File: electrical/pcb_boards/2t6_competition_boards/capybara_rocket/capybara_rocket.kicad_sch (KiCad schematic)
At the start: 77 parts, among them J1 3.6V Battery, J10 Elevator, J11 SparkFun MAX-M10S, J12 Aileron 1, J13 Aileron 2, J14 Ground Camera, J15 Payload Camera, J16 DC Motor, J2 1.2V Battery, J3 3.6V Switch, J4 1.2V Switch, J5 LED, J6 NC, J7 CC, J8 VL53L1-SATEL, J9 Egg, U1 NE555P, U10 EEPROM, U11 STM32 NUCLEO-G431KB, U12 SparkFun XBee Explorer, U13 MAX756CPA+, U2 DS1307+, U3 Adafruit BNO085, U4 LTC3536, U5 MP3414, U6 Adafruit BMP581, U7 INA219, U8 DRV8212DRLR, U9 SN74LVC1G04DBVR, Y1 AB38T-32.768KHZ

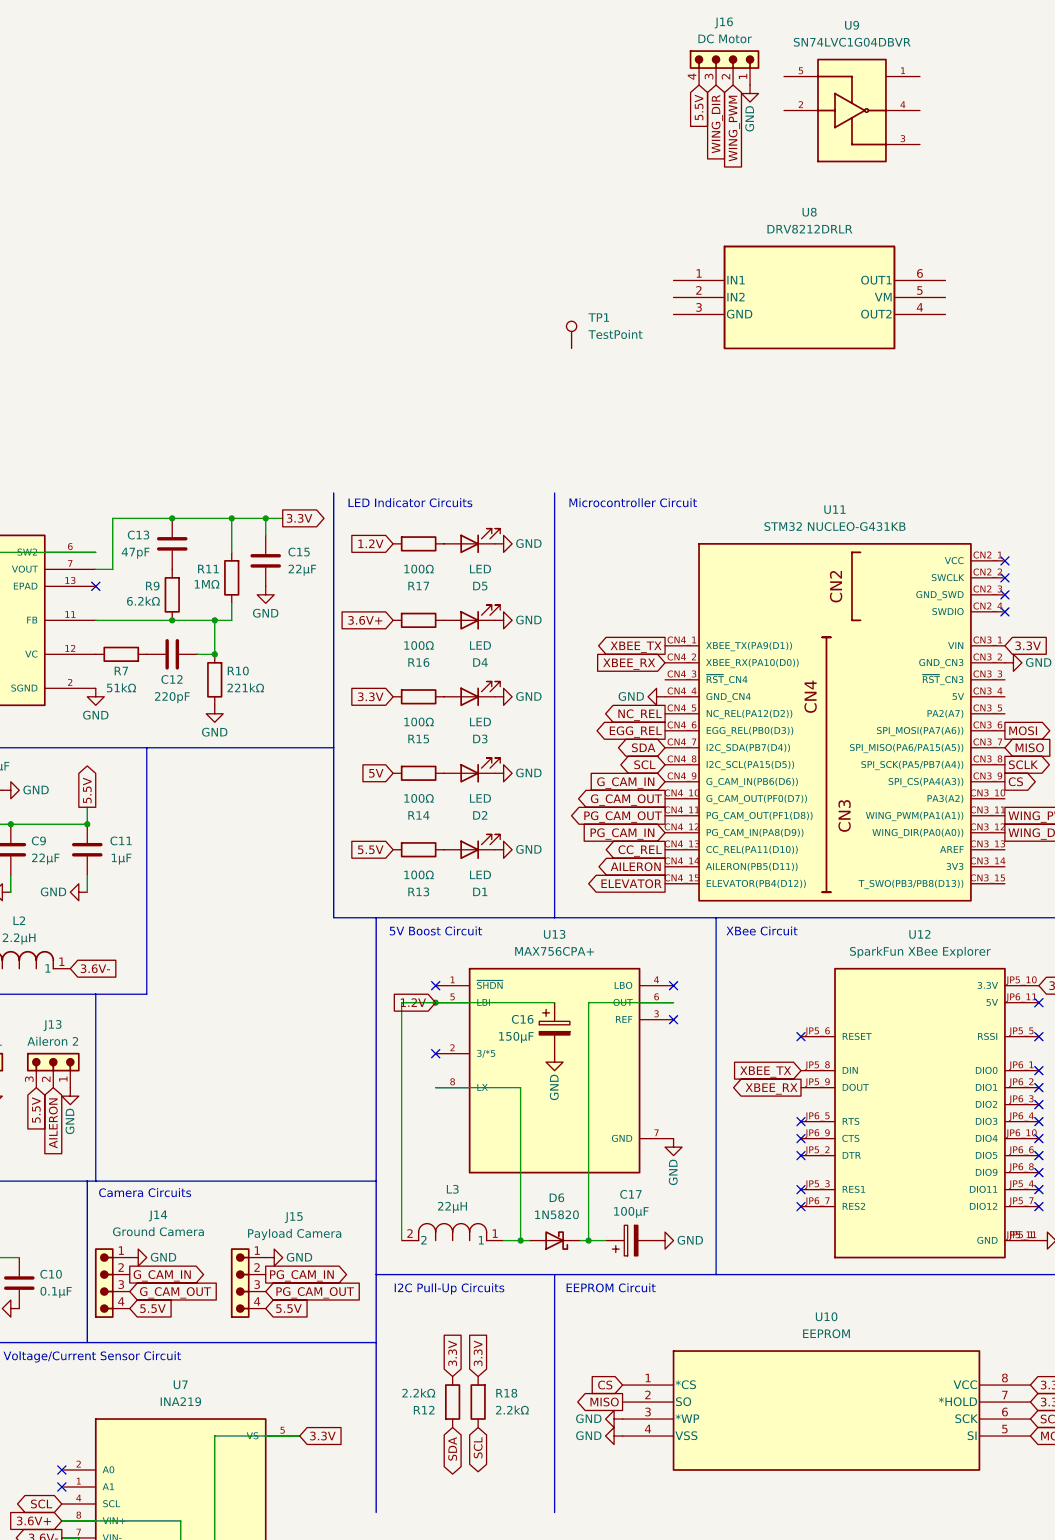
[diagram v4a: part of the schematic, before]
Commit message: Updates on component placements
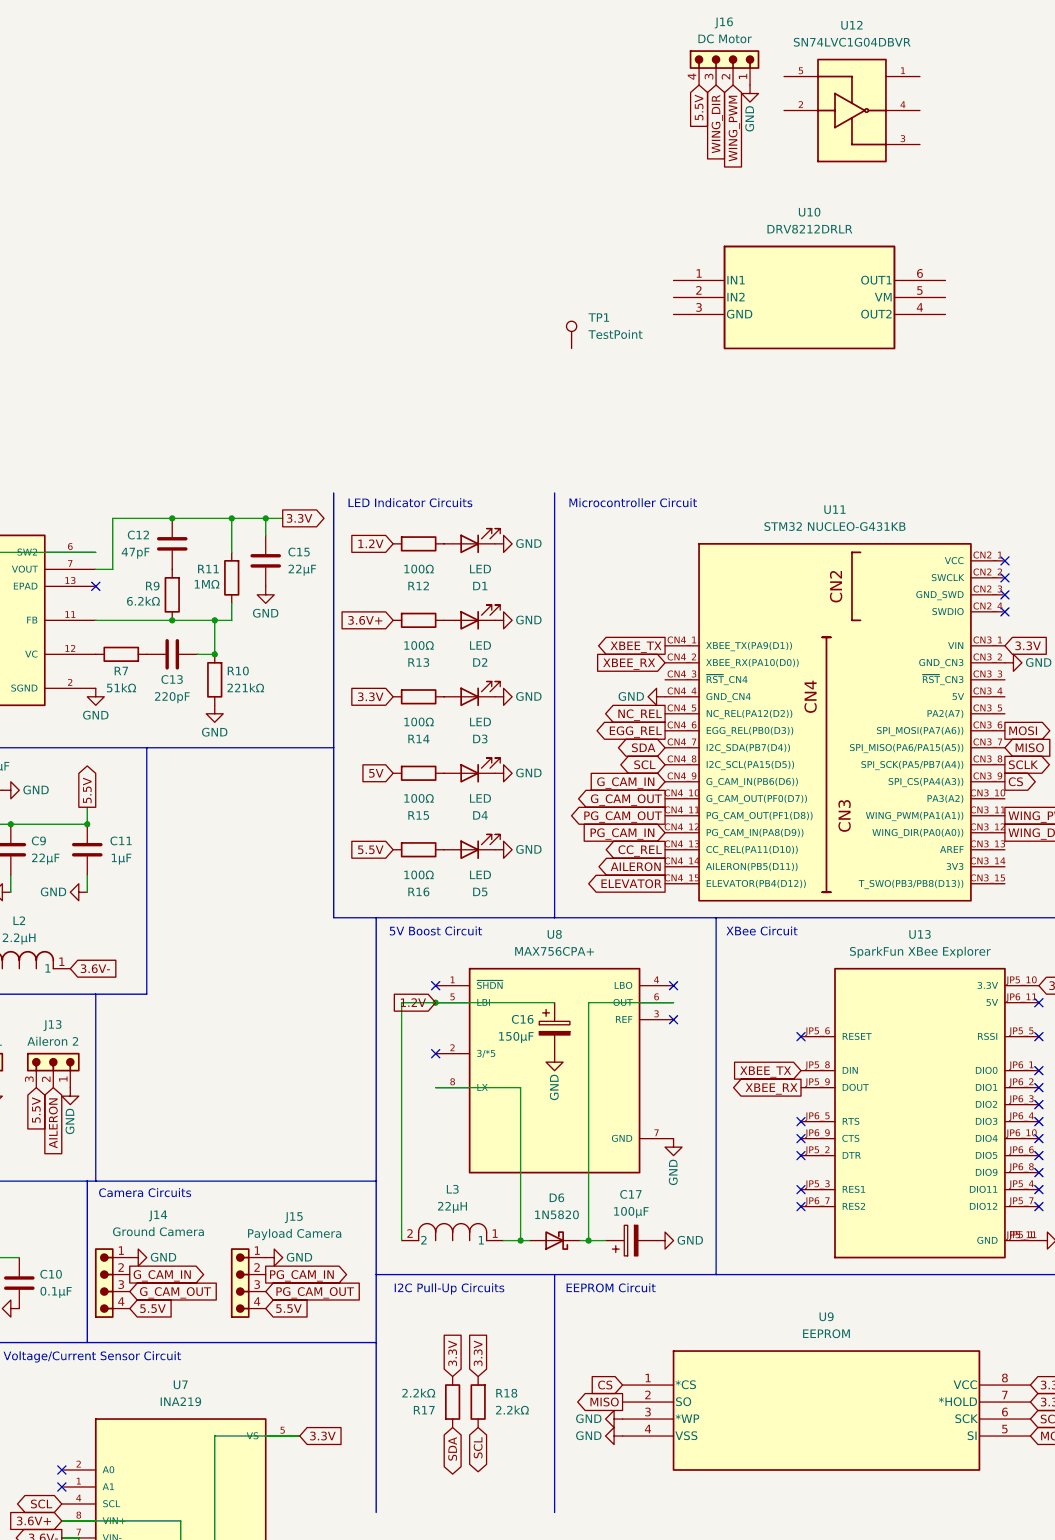
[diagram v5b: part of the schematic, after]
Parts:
- renumbered C13 to C12, C12 to C13, D5 to D1, D4 to D2, D2 to D4, D1 to D5, R17 to R12, R16 to R13, R15 to R14, R14 to R15, R13 to R16, R12 to R17, U8 to U10, U9 to U12, U12 to U13, U13 to U8, U10 to U9
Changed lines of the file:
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@@
 		(on_board yes)
 		(dnp no)
-		(property "Reference" "#PWR044"
+		(property "Reference" "#PWR048"
 			(at 200.66 66.04 0)
 			(effects
@@
 			(project "capybara_rocket"
 				(path "/401cca29-8a99-4116-a8ac-f330975a064c"
-					(reference "#PWR044")
+					(reference "#PWR048")
 					(unit 1)
 				)
@@
 		(on_board yes)
 		(dnp no)
-		(property "Reference" "#PWR040"
+		(property "Reference" "#PWR041"
 			(at 166.37 127 0)
 			(effects
@@
 			(project "capybara_rocket"
 				(path "/401cca29-8a99-4116-a8ac-f330975a064c"
-					(reference "#PWR040")
+					(reference "#PWR041")
 					(unit 1)
 				)
@@
 		(dnp no)
 		(fields_autoplaced yes)
-		(property "Reference" "D1"
+		(property "Reference" "D5"
 			(at 192.0875 72.39 0)
 			(effects
@@
 			(project ""
 				(path "/401cca29-8a99-4116-a8ac-f330975a064c"
-					(reference "D1")
+					(reference "D5")
 					(unit 1)
 				)
@@
 		(dnp no)
 		(fields_autoplaced yes)
-		(property "Reference" "U12"
+		(property "Reference" "U13"
 			(at 257.81 78.74 0)
 			(effects
@@
 			(project ""
 				(path "/401cca29-8a99-4116-a8ac-f330975a064c"
-					(reference "U12")
+					(reference "U13")
 					(unit 1)
 				)
@@
 		(on_board yes)
 		(dnp no)
-		(property "Reference" "R12"
+		(property "Reference" "R17"
 			(at 185.42 149.8601 0)
 			(effects
@@
 			(project "capybara_rocket"
 				(path "/401cca29-8a99-4116-a8ac-f330975a064c"
-					(reference "R12")
+					(reference "R17")
 					(unit 1)
 				)
@@
 		(dnp no)
 		(fields_autoplaced yes)
-		(property "Reference" "D2"
+		(property "Reference" "D4"
 			(at 192.0875 60.96 0)
 			(effects
@@
 			(project "capybara_rocket"
 				(path "/401cca29-8a99-4116-a8ac-f330975a064c"
-					(reference "D2")
+					(reference "D4")
 					(unit 1)
 				)
@@
 		(on_board yes)
 		(dnp no)
-		(property "Reference" "#PWR042"
+		(property "Reference" "#PWR040"
 			(at 160.02 33.02 0)
 			(effects
@@
 			(project "capybara_rocket"
 				(path "/401cca29-8a99-4116-a8ac-f330975a064c"
-					(reference "#PWR042")
+					(reference "#PWR040")
 					(unit 1)
 				)
@@
 		(on_board yes)
 		(dnp no)
-		(property "Reference" "#PWR049"
+		(property "Reference" "#PWR055"
 			(at 232.41 -41.91 0)
 			(effects
@@
 			(project "capybara_rocket"
 				(path "/401cca29-8a99-4116-a8ac-f330975a064c"
-					(reference "#PWR049")
+					(reference "#PWR055")
 					(unit 1)
 				)
@@
 		(on_board yes)
 		(dnp no)
-		(property "Reference" "#PWR055"
+		(property "Reference" "#PWR054"
 			(at 220.98 115.57 0)
 			(effects
@@
 			(project "capybara_rocket"
 				(path "/401cca29-8a99-4116-a8ac-f330975a064c"
-					(reference "#PWR055")
+					(reference "#PWR054")
 					(unit 1)
 				)
@@
 		(dnp no)
 		(fields_autoplaced yes)
-		(property "Reference" "D5"
+		(property "Reference" "D1"
 			(at 192.0875 26.67 0)
 			(effects
@@
 			(project "capybara_rocket"
 				(path "/401cca29-8a99-4116-a8ac-f330975a064c"
-					(reference "D5")
+					(reference "D1")
 					(unit 1)
 				)
@@
 		(dnp no)
 		(fields_autoplaced yes)
-		(property "Reference" "R13"
+		(property "Reference" "R16"
 			(at 182.88 72.39 90)
 			(effects
@@
 			(project "capybara_rocket"
 				(path "/401cca29-8a99-4116-a8ac-f330975a064c"
-					(reference "R13")
+					(reference "R16")
 					(unit 1)
 				)
@@
 		(on_board yes)
 		(dnp no)
-		(property "Reference" "#PWR053"
+		(property "Reference" "#PWR056"
 			(at 276.86 38.1 0)
 			(effects
@@
 			(project "capybara_rocket"
 				(path "/401cca29-8a99-4116-a8ac-f330975a064c"
-					(reference "#PWR053")
+					(reference "#PWR056")
 					(unit 1)
 				)
@@
 		(dnp no)
 		(fields_autoplaced yes)
-		(property "Reference" "R16"
+		(property "Reference" "R13"
 			(at 182.88 38.1 90)
 			(effects
@@
 			(project "capybara_rocket"
 				(path "/401cca29-8a99-4116-a8ac-f330975a064c"
-					(reference "R16")
+					(reference "R13")
 					(unit 1)
 				)
@@
 		(dnp no)
 		(fields_autoplaced yes)
-		(property "Reference" "R14"
+		(property "Reference" "R15"
 			(at 182.88 60.96 90)
 			(effects
@@
 			(project "capybara_rocket"
 				(path "/401cca29-8a99-4116-a8ac-f330975a064c"
-					(reference "R14")
+					(reference "R15")
 					(unit 1)
 				)
@@
 		(on_board yes)
 		(dnp no)
-		(property "Reference" "#PWR057"
+		(property "Reference" "#PWR049"
 			(at 203.2 102.87 0)
 			(effects
@@
 			(project "capybara_rocket"
 				(path "/401cca29-8a99-4116-a8ac-f330975a064c"
-					(reference "#PWR057")
+					(reference "#PWR049")
 					(unit 1)
 				)
@@
 		(on_board yes)
 		(dnp no)
-		(property "Reference" "C13"
+		(property "Reference" "C12"
 			(at 142.748 19.05 0)
 			(effects
@@
 			(project "capybara_rocket"
 				(path "/401cca29-8a99-4116-a8ac-f330975a064c"
-					(reference "C13")
+					(reference "C12")
 					(unit 1)
 				)
@@
 		(dnp no)
 		(fields_autoplaced yes)
-		(property "Reference" "U8"
+		(property "Reference" "U10"
 			(at 241.3 -29.21 0)
 			(effects
@@
 			(project ""
 				(path "/401cca29-8a99-4116-a8ac-f330975a064c"
-					(reference "U8")
+					(reference "U10")
 					(unit 1)
 				)
@@
 		(on_board yes)
 		(dnp no)
-		(property "Reference" "#PWR056"
+		(property "Reference" "#PWR052"
 			(at 224.79 124.46 0)
 			(effects
@@
 			(project "capybara_rocket"
 				(path "/401cca29-8a99-4116-a8ac-f330975a064c"
-					(reference "#PWR056")
+					(reference "#PWR052")
 					(unit 1)
 				)
@@
 		(on_board yes)
 		(dnp no)
-		(property "Reference" "#PWR052"
+		(property "Reference" "#PWR053"
 			(at 213.36 43.18 0)
 			(effects
@@
 			(project "capybara_rocket"
 				(path "/401cca29-8a99-4116-a8ac-f330975a064c"
-					(reference "#PWR052")
+					(reference "#PWR053")
 					(unit 1)
 				)
@@
 		(dnp no)
 		(fields_autoplaced yes)
-		(property "Reference" "R15"
+		(property "Reference" "R14"
 			(at 182.88 49.53 90)
 			(effects
@@
 			(project "capybara_rocket"
 				(path "/401cca29-8a99-4116-a8ac-f330975a064c"
-					(reference "R15")
+					(reference "R14")
 					(unit 1)
 				)
@@
 		(dnp no)
 		(fields_autoplaced yes)
-		(property "Reference" "U10"
+		(property "Reference" "U9"
 			(at 243.84 135.89 0)
 			(effects
@@
 			(project ""
 				(path "/401cca29-8a99-4116-a8ac-f330975a064c"
-					(reference "U10")
+					(reference "U9")
 					(unit 1)
 				)
@@
 		(on_board yes)
 		(dnp no)
-		(property "Reference" "C12"
+		(property "Reference" "C13"
 			(at 146.05 40.64 90)
 			(effects
@@
 			(project "capybara_rocket"
 				(path "/401cca29-8a99-4116-a8ac-f330975a064c"
-					(reference "C12")
+					(reference "C13")
 					(unit 1)
 				)
@@
 		(dnp no)
 		(fields_autoplaced yes)
-		(property "Reference" "U9"
+		(property "Reference" "U12"
 			(at 247.65 -57.15 0)
 			(effects
@@
 			(project ""
 				(path "/401cca29-8a99-4116-a8ac-f330975a064c"
-					(reference "U9")
+					(reference "U12")
 					(unit 1)
 				)
@@
 		(on_board yes)
 		(dnp no)
-		(property "Reference" "#PWR054"
+		(property "Reference" "#PWR057"
 			(at 281.94 124.46 0)
 			(effects
@@
 			(project "capybara_rocket"
 				(path "/401cca29-8a99-4116-a8ac-f330975a064c"
-					(reference "#PWR054")
+					(reference "#PWR057")
 					(unit 1)
 				)
@@
 		(on_board yes)
 		(dnp no)
-		(property "Reference" "#PWR045"
+		(property "Reference" "#PWR047"
 			(at 200.66 54.61 0)
 			(effects
@@
 			(project "capybara_rocket"
 				(path "/401cca29-8a99-4116-a8ac-f330975a064c"
-					(reference "#PWR045")
+					(reference "#PWR047")
 					(unit 1)
 				)
@@
 		(dnp no)
 		(fields_autoplaced yes)
-		(property "Reference" "U13"
+		(property "Reference" "U8"
 			(at 203.2 78.74 0)
 			(effects
@@
 			(project ""
 				(path "/401cca29-8a99-4116-a8ac-f330975a064c"
-					(reference "U13")
+					(reference "U8")
 					(unit 1)
 				)
@@
 		(on_board yes)
 		(dnp no)
-		(property "Reference" "#PWR041"
+		(property "Reference" "#PWR042"
 			(at 166.37 186.69 0)
 			(effects
@@
 			(project "capybara_rocket"
 				(path "/401cca29-8a99-4116-a8ac-f330975a064c"
-					(reference "#PWR041")
+					(reference "#PWR042")
 					(unit 1)
 				)
@@
 		(dnp no)
 		(fields_autoplaced yes)
-		(property "Reference" "R17"
+		(property "Reference" "R12"
 			(at 182.88 26.67 90)
 			(effects
@@
 			(project "capybara_rocket"
 				(path "/401cca29-8a99-4116-a8ac-f330975a064c"
-					(reference "R17")
+					(reference "R12")
 					(unit 1)
 				)
@@
 		(dnp no)
 		(fields_autoplaced yes)
-		(property "Reference" "D4"
+		(property "Reference" "D2"
 			(at 192.0875 38.1 0)
 			(effects
@@
 			(project "capybara_rocket"
 				(path "/401cca29-8a99-4116-a8ac-f330975a064c"
-					(reference "D4")
+					(reference "D2")
 					(unit 1)
 				)
@@
 		(on_board yes)
 		(dnp no)
-		(property "Reference" "#PWR048"
+		(property "Reference" "#PWR044"
 			(at 200.66 20.32 0)
 			(effects
@@
 			(project "capybara_rocket"
 				(path "/401cca29-8a99-4116-a8ac-f330975a064c"
-					(reference "#PWR048")
+					(reference "#PWR044")
 					(unit 1)
 				)
@@
 		(on_board yes)
 		(dnp no)
-		(property "Reference" "#PWR047"
+		(property "Reference" "#PWR045"
 			(at 200.66 31.75 0)
 			(effects
@@
 			(project "capybara_rocket"
 				(path "/401cca29-8a99-4116-a8ac-f330975a064c"
-					(reference "#PWR047")
+					(reference "#PWR045")
 					(unit 1)
 				)
